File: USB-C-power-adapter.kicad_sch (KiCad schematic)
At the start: 54 parts, among them Q1 SQS401EN-T1_BE3, U1 STUSB4500_QFN, U2 SIC477ED-T1-GE3

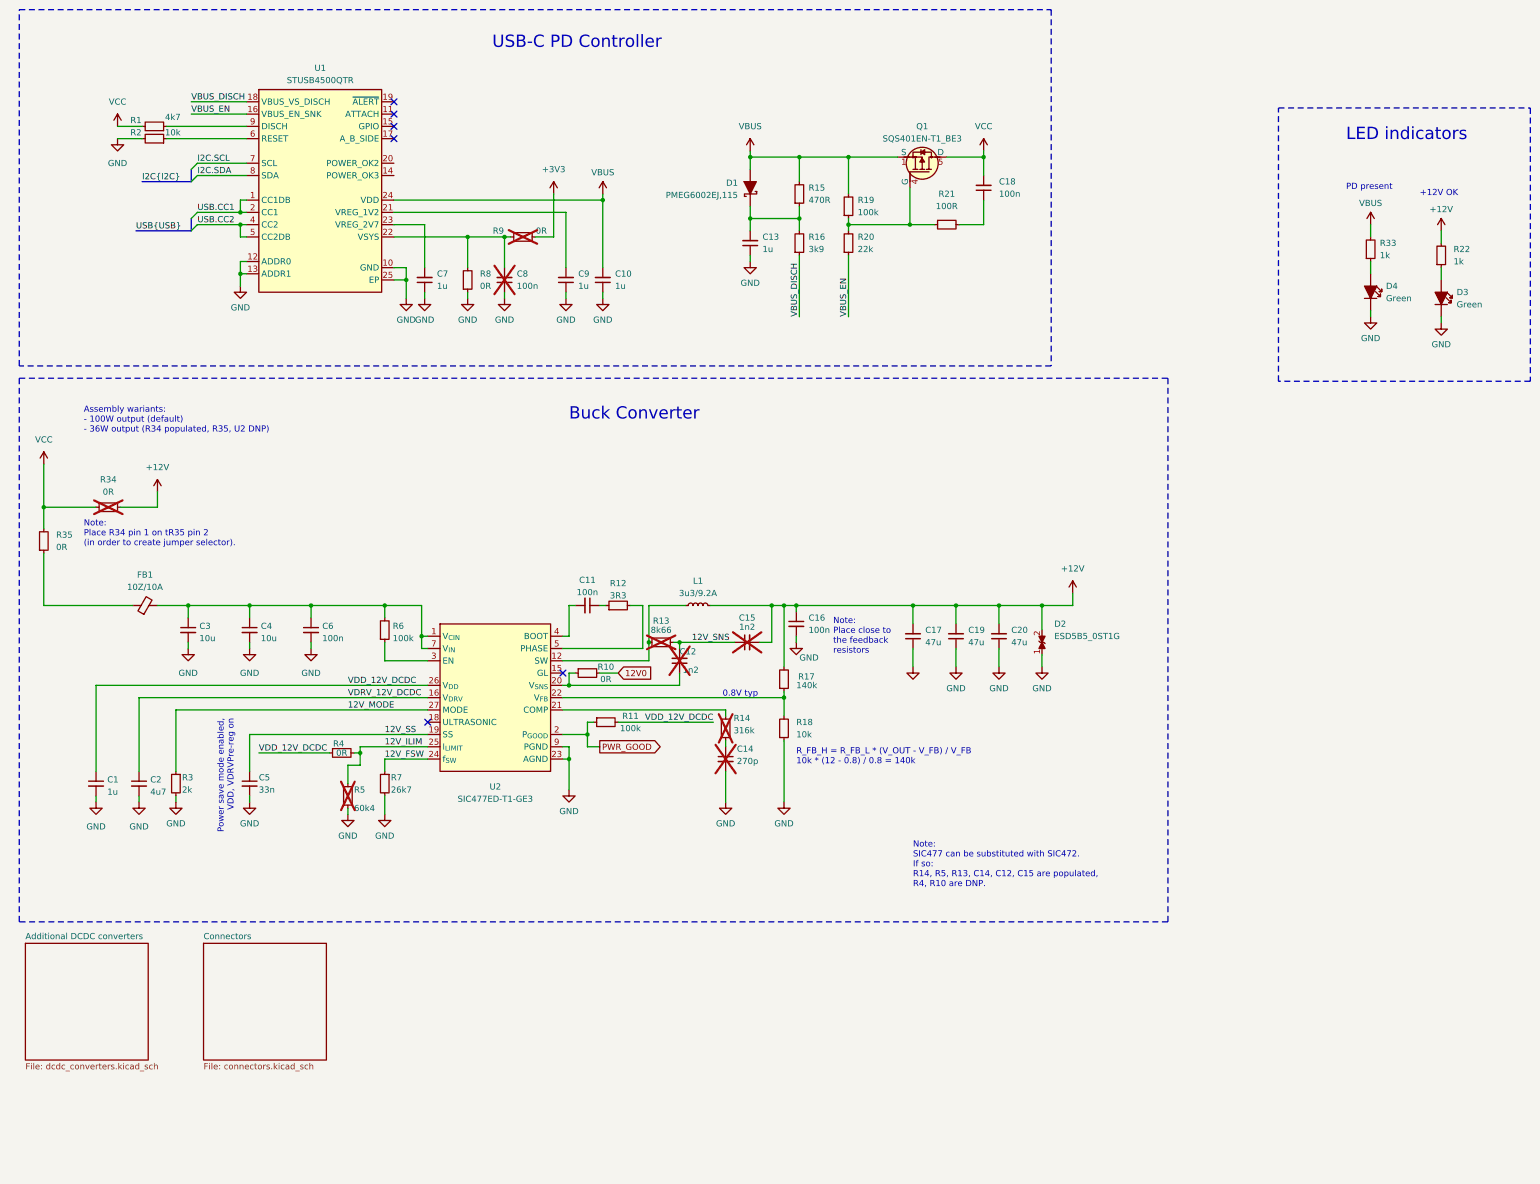
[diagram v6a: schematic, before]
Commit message: [#57006] Change L1
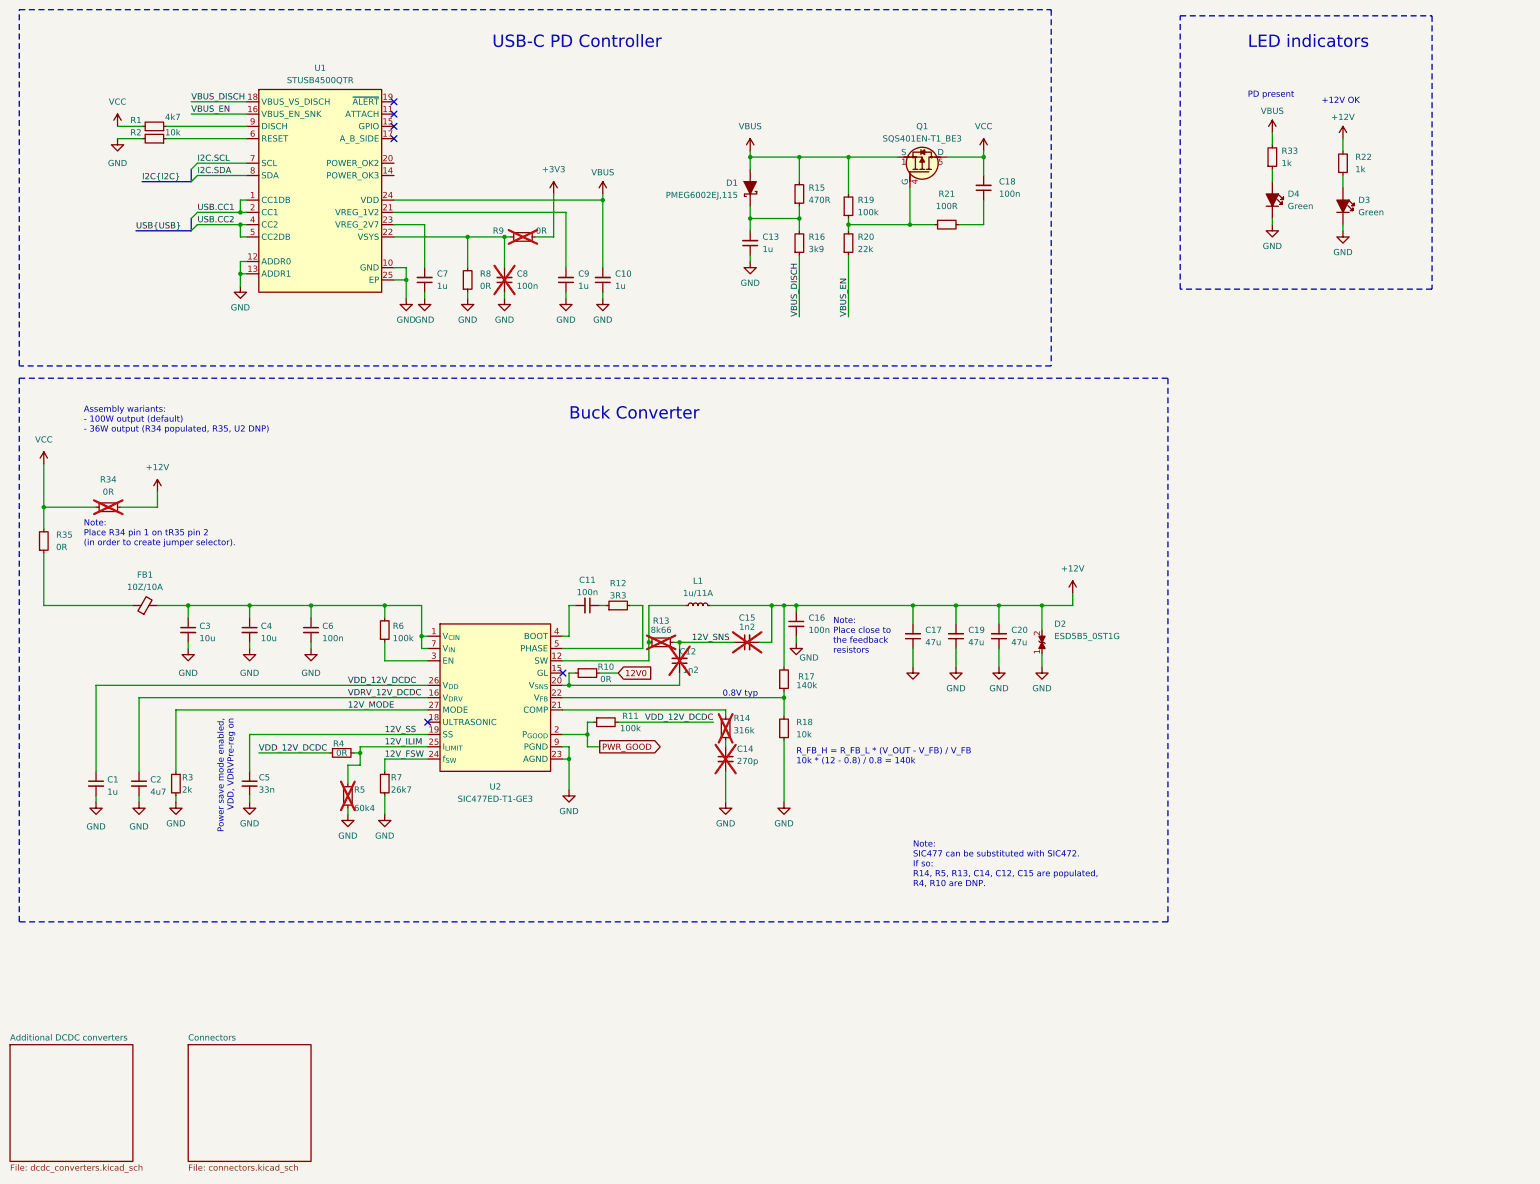
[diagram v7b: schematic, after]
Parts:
- removed L1: L_3u3_9.2A_Vishay-IHLP-3232DZ-01, antmicro-footprints:L_Vishay-IHLP3232DZ, symbol antmicroFixedInductors:L_3u3_9.2A_Vishay-IHLP-3232DZ-01
- added L1: L_1u_11A_Coilcraft-XFL4020, antmicro-footprints:L_Coilcraft-XFL4020, symbol antmicroFixedInductors:L_1u_11A_Coilcraft-XFL4020
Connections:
- net +12V: now also L1.2
- net at R13.1, U2.12 (SW), U2.13 (SW)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: now also L1.1
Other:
- moved on the sheet: D3, D4, R22, R33

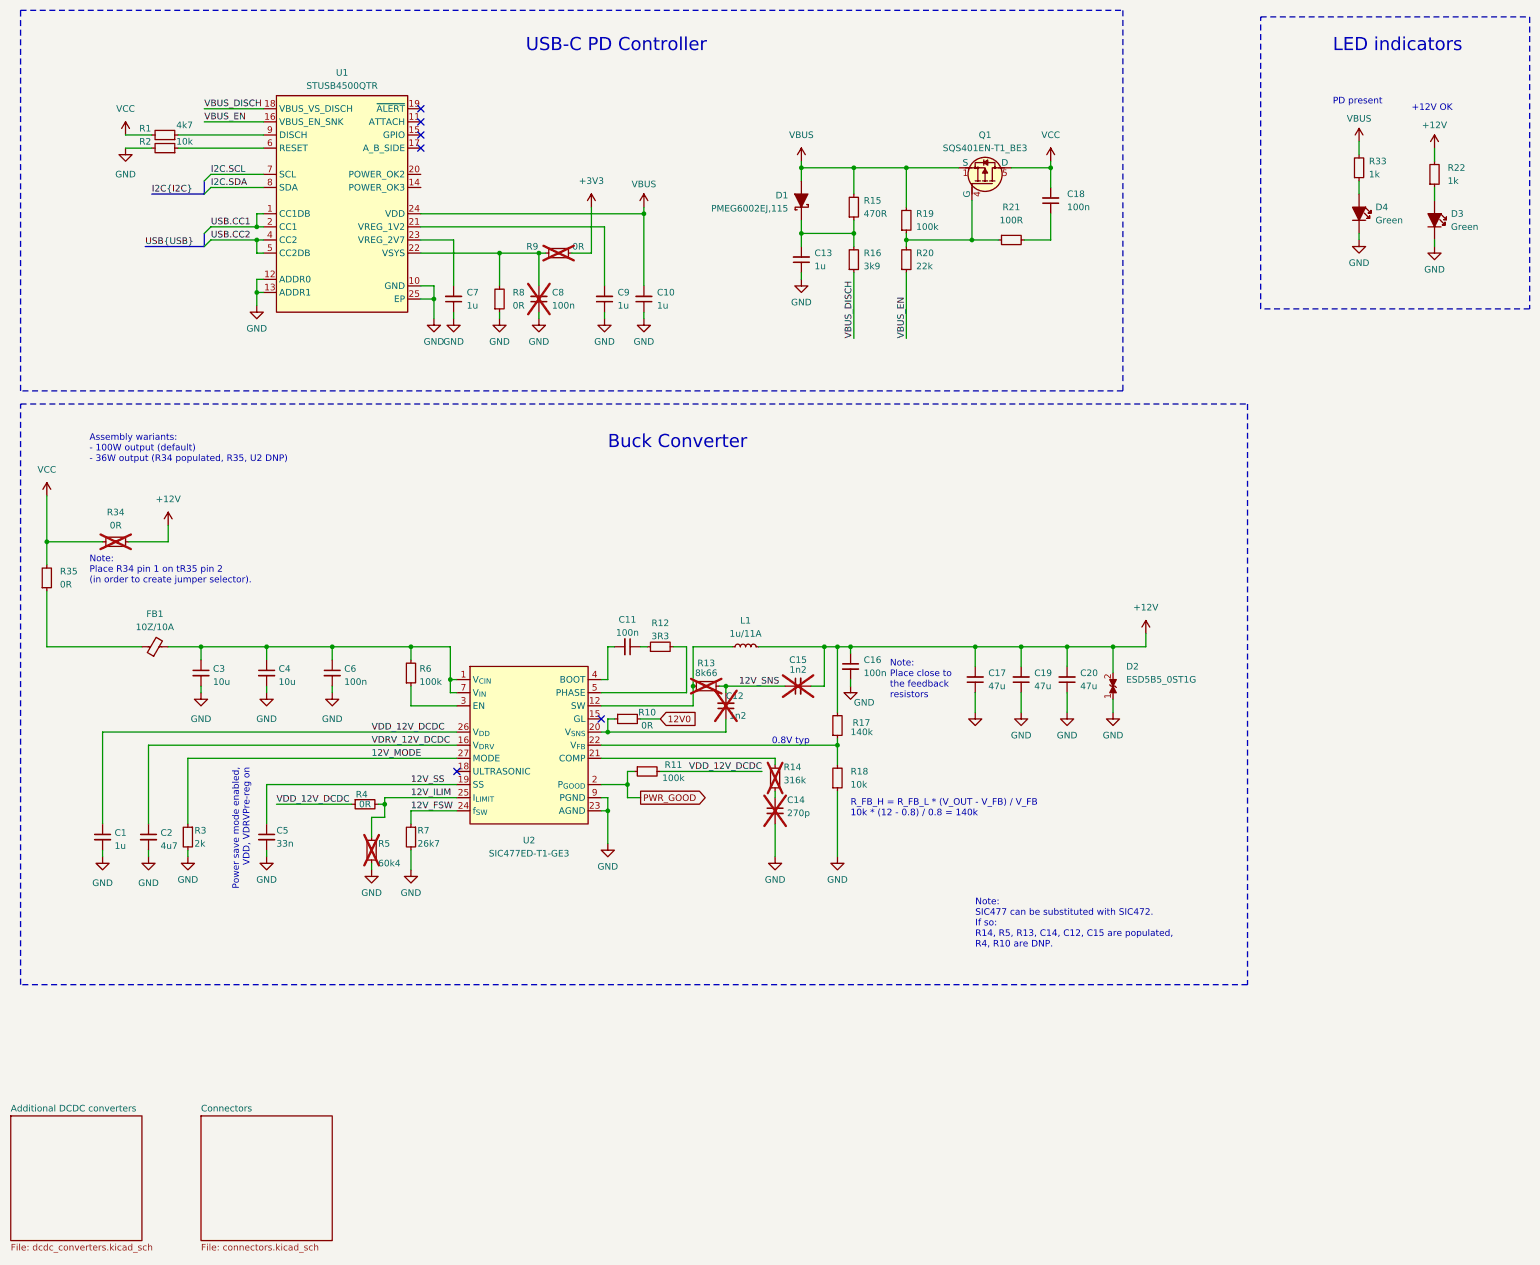
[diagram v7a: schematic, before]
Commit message: [#57006] Add a TVS diode on output
Move power components to a new sheet
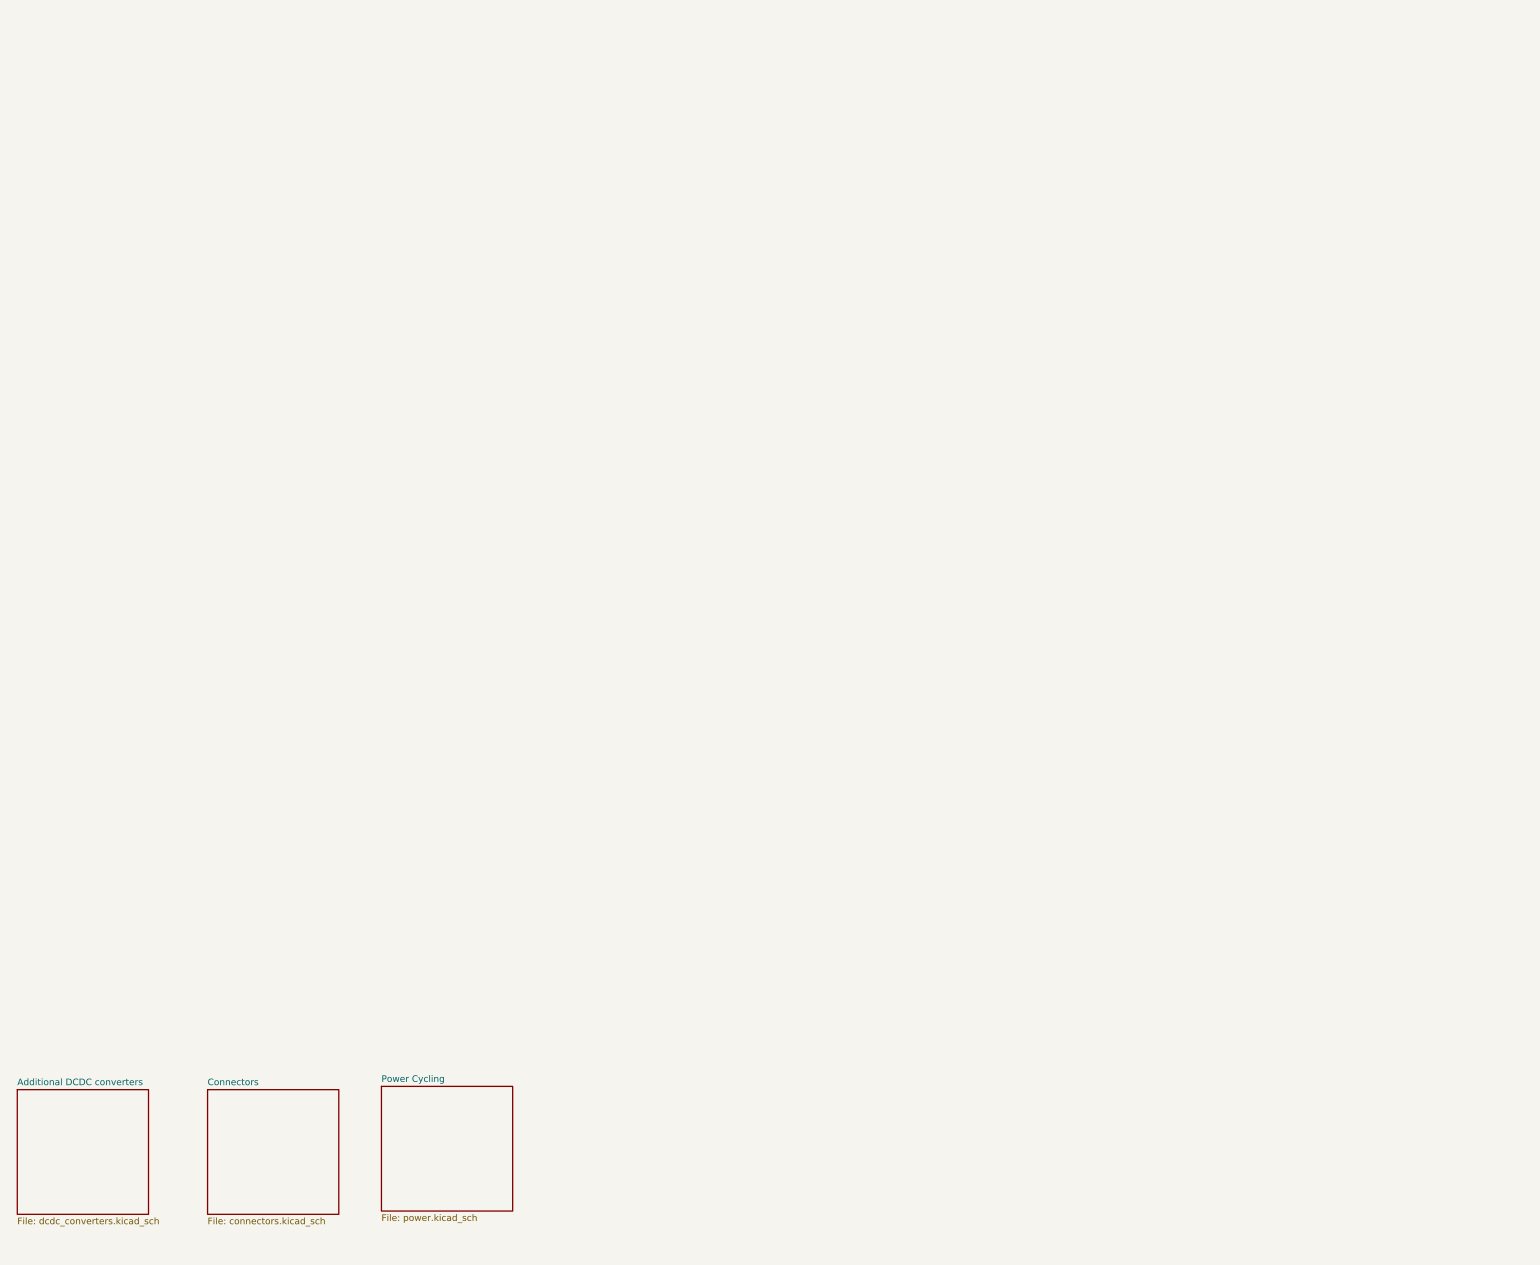
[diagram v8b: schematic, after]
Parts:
- removed C1, C10, C13, C7, C9: C_1u_0402, antmicro-footprints:C_0402_1005Metric, symbol antmicroCapacitors0402:C_1u_0402
- removed C11, C16, C8: C_100n_0402, antmicro-footprints:C_0402_1005Metric, symbol antmicroCapacitors0402:C_100n_0402
- removed C12, C15: C_1n2_50V_0402, antmicro-footprints:C_0402_1005Metric, symbol antmicroCapacitors0402:C_1n2_50V_0402
- removed C14: C_270p_25V_0402, antmicro-footprints:C_0402_1005Metric, symbol antmicroCapacitors0402:C_270p_25V_0402
- removed C17, C19, C20: C_47u_16V_1206, antmicro-footprints:C_1206_3216Metric, symbol antmicroCapacitorsmisc:C_47u_16V_1206
- removed C18: C_100n_50V_X8L_0402, antmicro-footprints:C_0402_1005Metric, symbol antmicroCapacitors0402:C_100n_50V_X8L_0402
- removed C2: C_4u7_0603, antmicro-footprints:C_0603_1608Metric, symbol antmicroCapacitors0603:C_4u7_0603
- removed C3, C4: C_10u_1206_50V, antmicro-footprints:C_1206_3216Metric, symbol antmicroCapacitorsmisc:C_10u_1206_50V
- removed C5: C_33n_0402, antmicro-footprints:C_0402_1005Metric, symbol antmicroCapacitors0402:C_33n_0402
- removed C6: C_100n_50V_0402, antmicro-footprints:C_0402_1005Metric, symbol antmicroCapacitorsmisc:C_100n_50V_0402
- removed D1: PMEG6002EJ,115, antmicro-footprints:D_SOD-323F, symbol antmicroDiodesRectifiersSingle:PMEG6002EJ,115
- removed D2: ESD5B5_0ST1G, antmicro-footprints:SOD-523_NP, symbol antmicroTVSDiodes:ESD5B5_0ST1G
- removed D3, D4: LED_G_0603_LG_L29K-G2J1-24-Z, antmicro-footprints:LED_0603_1608Metric_G, symbol antmicroLEDIndicationDiscrete:LED_G_0603_LG_L29K-G2J1-24-Z
- removed FB1: FB_10Z_10A_WE-MPSB_1206, antmicro-footprints:FB_1206_3216Metric, symbol antmicroFerriteBeadsandChips:FB_10Z_10A_WE-MPSB_1206
- removed L1: L_1u_11A_Coilcraft-XFL4020, antmicro-footprints:L_Coilcraft-XFL4020, symbol antmicroFixedInductors:L_1u_11A_Coilcraft-XFL4020
- removed Q1: SQS401EN-T1_BE3, antmicro-footprints:Vishay_PowerPAK_1212-8_Single, symbol antmicroTransistorsFETsMOSFETsSingle:SQS401EN-T1_BE3
- removed R1: R_4k7_0805, antmicro-footprints:R_0805_2012Metric, symbol antmicroResistorsmisc:R_4k7_0805
- removed R10, R4, R8, R9: R_0R_0402, antmicro-footprints:R_0402_1005Metric, symbol antmicroResistors0402:R_0R_0402
- removed R11, R19, R6: R_100k_0402, antmicro-footprints:R_0402_1005Metric, symbol antmicroResistors0402:R_100k_0402
- removed R12: R_3R3_0402, antmicro-footprints:R_0402_1005Metric, symbol antmicroResistors0402:R_3R3_0402
- removed R13: R_8k66_0402, antmicro-footprints:R_0402_1005Metric, symbol antmicroResistors0402:R_8k66_0402
- removed R14: R_316k_0402, antmicro-footprints:R_0402_1005Metric, symbol antmicroResistors0402:R_316k_0402
- removed R15: R_470R_0603, antmicro-footprints:R_0603_1608Metric, symbol antmicroResistors0603:R_470R_0603
- removed R16: R_3k9_0603, antmicro-footprints:R_0603_1608Metric, symbol antmicroResistors0603:R_3k9_0603
- removed R17: R_140k_0.1%_0402, antmicro-footprints:R_0402_1005Metric, symbol antmicroResistors0402:R_140k_0.1%_0402
- removed R18: R_10k_0.1%_0402, antmicro-footprints:R_0402_1005Metric, symbol antmicroResistors0402:R_10k_0.1%_0402
- removed R2: R_10k_0402, antmicro-footprints:R_0402_1005Metric, symbol antmicroResistors0402:R_10k_0402
- removed R20: R_22k_0402, antmicro-footprints:R_0402_1005Metric, symbol antmicroResistors0402:R_22k_0402
- removed R21: R_100R_0402, antmicro-footprints:R_0402_1005Metric, symbol antmicroResistors0402:R_100R_0402
- removed R22, R33: R_2k2_0402, antmicro-footprints:R_0402_1005Metric, symbol antmicroResistors0402:R_1k_0402
- removed R3: R_2k_0402, antmicro-footprints:R_0402_1005Metric, symbol antmicroResistors0402:R_2k_0402
- removed R34, R35: R_0R_0805, antmicro-footprints:R_0805_2012Metric, symbol antmicroResistorsmisc:R_0R_0805
- removed R5: R_60k4_0402, antmicro-footprints:R_0402_1005Metric, symbol antmicroResistors0402:R_60k4_0402
- removed R7: R_26k7_0402, antmicro-footprints:R_0402_1005Metric, symbol antmicroResistors0402:R_26k7_0402
- removed U1: STUSB4500_QFN, antmicro-footprints:QFN-24-1EP_4x4mm_P0.5_EP2.1x2.1mm, symbol antmicroPMICPowerDistributionSwitchesLoadDrivers:STUSB4500_QFN
- removed U2: SIC477ED-T1-GE3, antmicro-footprints:SIC47XED-T1-GE3, symbol antmicroDCDCConverters:SIC477ED-T1-GE3
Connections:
- no-connect marks 6 -> 0
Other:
- added sheet Power Cycling (power.kicad_sch)
- note removed: "+12V OK"
- note removed: "0.8V typ"
- note removed: "Assembly wariants: - 100W output (default) - 36W output (R34 populated, R35, U2 DNP)"
- note removed: "Buck Converter"
- note removed: "LED indicators"
- note removed: "Note: Place R34 pin 1 on tR35 pin 2 (in order to create jumper selector)."
- note removed: "Note: Place close to the feedback resistors"
- note removed: "Note: SIC477 can be substituted with SIC472. If so: R14, R5, R13, C14, C12, C15 are populated, R4, R10 are DNP."
- note removed: "PD present"
- note removed: "Power save mode enabled, VDD, VDRVPre-reg on"
- note removed: "R_FB_H = R_FB_L * (V_OUT - V_FB) / V_FB 10k * (12 - 0.8) / 0.8 = 140k"
- note removed: "USB-C PD Controller"
